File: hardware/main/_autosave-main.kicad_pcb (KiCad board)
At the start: 2 copper layers, 120 parts, among them J1 RJ45, J2 RJ45, J401 USART, J601 RJ45, J602 RJ45, K1 DIPxx-1Axx-13x, K2 SANYOU_SRD_Form_C, Q1 Q_NPN_BEC, Q2 BCV27, Q3 BCV27, U1 LM324, U2 LM324, U201 MCP2551-I/SN, U202 MCP2515-xSO, U401 ATMEGA328P-PU, U501 LM7805, Y201 16MHz, Y401 16MHz

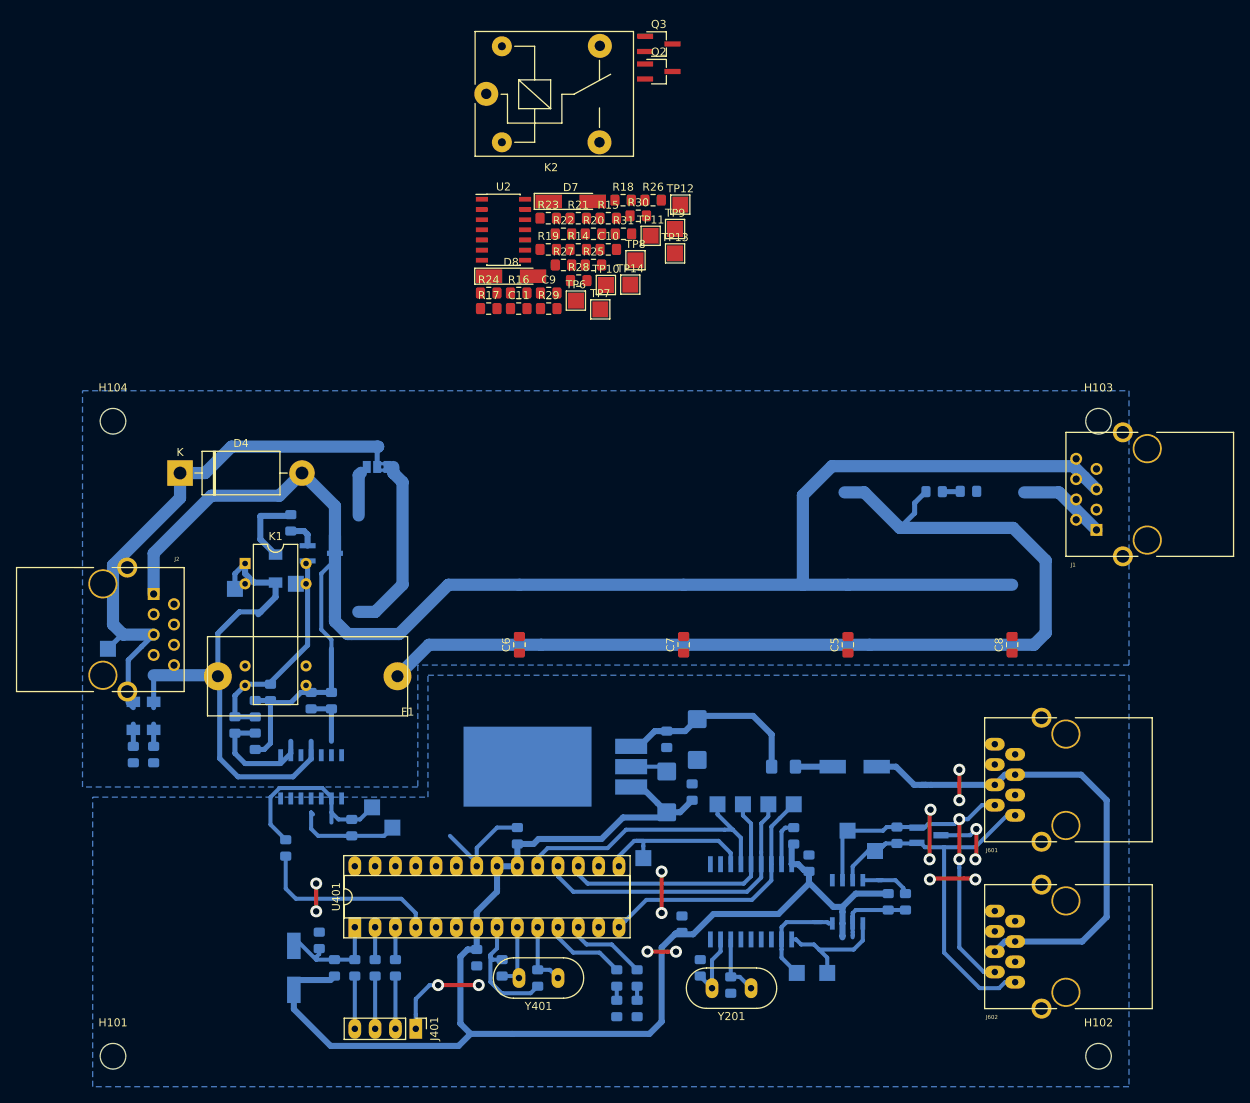
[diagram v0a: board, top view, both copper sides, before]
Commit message: Esquematico primeira versão Erro de referencia dos componentes na PCB com os do Esquematico solucionados
Pontos de teste adicionados
Alimentar o analog com +12V
Adicionar Snubber para os reles
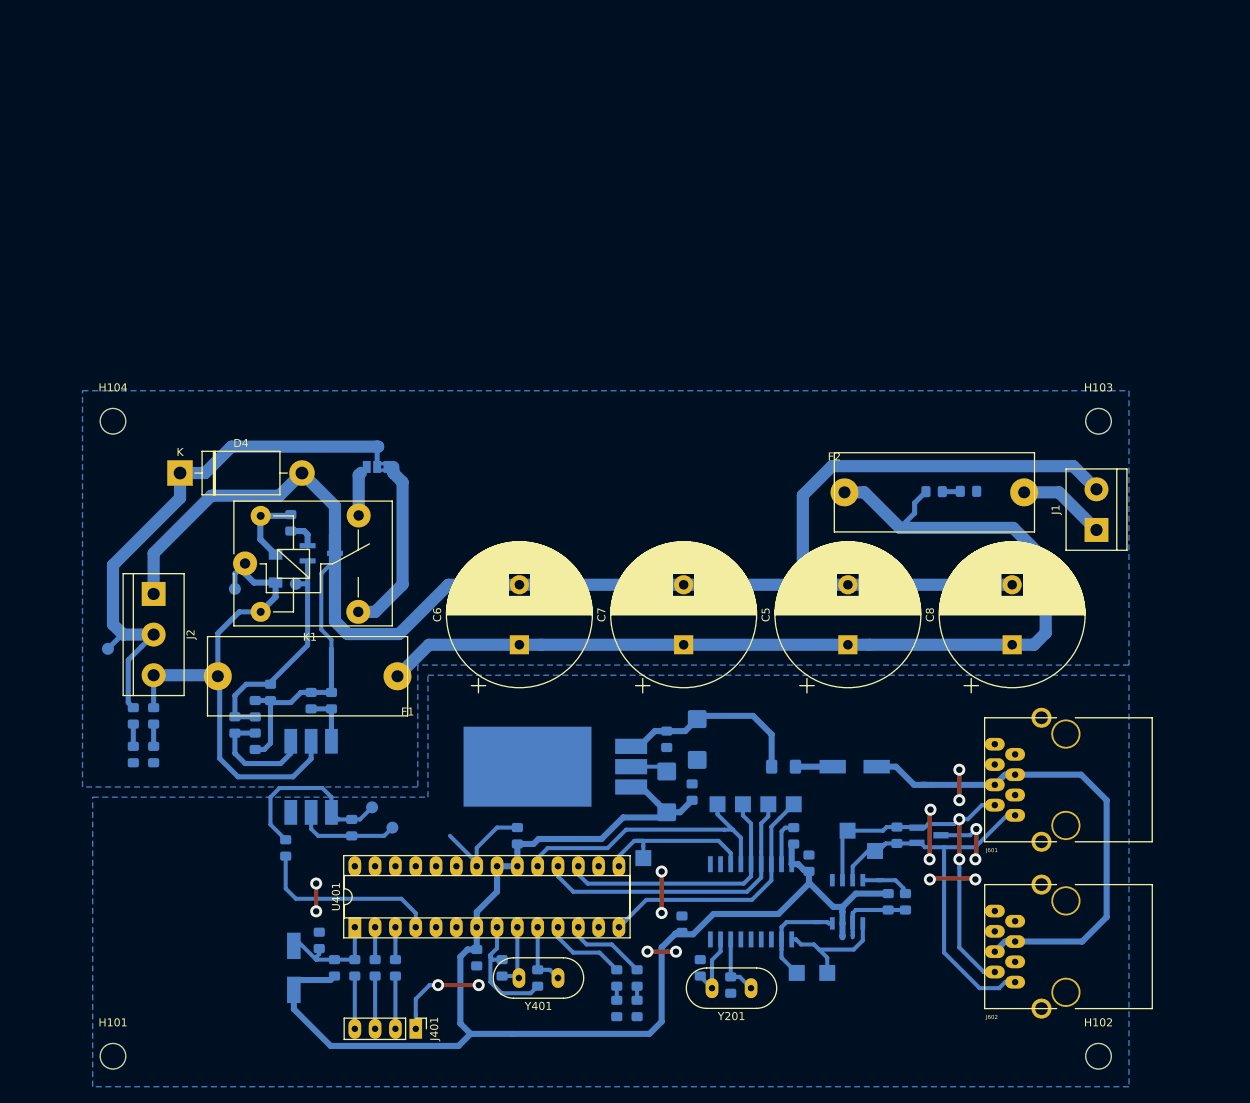
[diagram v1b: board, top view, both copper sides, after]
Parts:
- removed C10, C11, C9: 100n, Capacitor_SMD:C_0805_2012Metric_Pad1.15x1.40mm_HandSolder
- removed D7, D8: 4V7, Diode_SMD:D_MiniMELF_Handsoldering
- removed K2: SANYOU_SRD_Form_C, Relay_THT:Relay_SPDT_SANYOU_SRD_Series_Form_C
- removed Q2, Q3: BCV27, Package_TO_SOT_SMD:TSOT-23_HandSoldering
- removed R14, R15: 100k, Resistor_SMD:R_0805_2012Metric_Pad1.15x1.40mm_HandSolder
- removed R16, R17, R18, R19, R20, R21, R22, R23, R24, R25: 10k, Resistor_SMD:R_0805_2012Metric_Pad1.15x1.40mm_HandSolder
- removed R26, R27, R28, R29, R30, R31: 1k, Resistor_SMD:R_0805_2012Metric_Pad1.15x1.40mm_HandSolder
- removed TP10, TP9: op_a_out, TestPoint:TestPoint_Pad_2.0x2.0mm
- removed TP11, TP12: op_b_in+, TestPoint:TestPoint_Pad_2.0x2.0mm
- removed TP13, TP14: op_b_out, TestPoint:TestPoint_Pad_2.0x2.0mm
- removed TP6, TP8: op_a_in+, TestPoint:TestPoint_Pad_2.0x2.0mm
- removed TP7: op_a_in-, TestPoint:TestPoint_Pad_2.0x2.0mm
- removed U2: LM324, Package_SO:SOIC-14_3.9x8.7mm_P1.27mm
- added F2: 10A, KicadZeniteSolarLibrary18:Fuse_Holder_5x20, F.Cu at (170.2, 48.4)
- C1: value C_Small -> 100n
- C2: value 100n -> 1n
- C5, C6, C7, C8: value 100n -> 4700u 35V; footprint Capacitor_SMD:C_0805_2012Metric_Pad1.15x1.40mm_HandSolder -> Capacitor_THT:CP_Radial_D18.0mm_P7.50mm
- D1: value LL4148 -> G3mm; footprint Diode_SMD:D_MiniMELF -> LED_SMD:LED_0805_2012Metric_Pad1.15x1.40mm_HandSolder
- D3: value LL4148 -> R3mm; footprint Diode_SMD:D_MiniMELF -> LED_SMD:LED_0805_2012Metric_Pad1.15x1.40mm_HandSolder
- D4: value RED_LED -> MUR460
- D5: value GRN_LED -> G3mm
- F1: value Fuse Mega 200A -> 3A
- J1: value RJ45 -> Screw_Terminal_01x02; footprint KicadZeniteSolarLibrary18:RJ45_YH59_01 -> TerminalBlock:TerminalBlock_bornier-2_P5.08mm
- J2: value RJ45 -> Screw_Terminal_01x03; footprint KicadZeniteSolarLibrary18:RJ45_YH59_01 -> TerminalBlock:TerminalBlock_bornier-3_P5.08mm
- JP1: value Jp_TEST -> SolderJumper_3_Bridged12
- K1: value DIPxx-1Axx-13x -> coil: 12VDC, contact: 125V/10A; footprint Relay_THT:Relay_StandexMeder_DIP_LowProfile -> Relay_THT:Relay_SPDT_SANYOU_SRD_Series_Form_C
- Q1: value Q_NPN_BEC -> BCV27
- R1: value 1k2 -> 330R
- R2: value 1k2 -> NC
- R3: value 10k -> 1k2
- R4, R8: value 10k -> 1k
- R5: value 120 -> 10k
- R6: value 120 -> 120R
- R7: value 120 -> 1k
- TP1: value in- -> A1; footprint TestPoint:TestPoint_Pad_2.0x2.0mm -> TestPoint:TestPoint_Pad_D1.5mm
- TP2: value in+ -> K1; footprint TestPoint:TestPoint_Pad_2.0x2.0mm -> TestPoint:TestPoint_Pad_D1.5mm
- TP3: value in- -> 12V; footprint TestPoint:TestPoint_Pad_2.0x2.0mm -> TestPoint:TestPoint_Pad_D1.5mm
- TP4: value in+ -> B1; footprint TestPoint:TestPoint_Pad_2.0x2.0mm -> TestPoint:TestPoint_Pad_D1.5mm
- TP5: value op_a_in- -> OUT1; footprint TestPoint:TestPoint_Pad_2.0x2.0mm -> TestPoint:TestPoint_Pad_D1.5mm
- U1: value LM324 -> 4N25; footprint Package_SO:SOIC-14_3.9x8.7mm_P1.27mm -> Package_DIP:DIP-6_W8.89mm_SMDSocket_LongPads
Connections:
- net /MCU/CAN_CTRL renamed Net-(U401-Pad23)
- net /MCU/RL_OFF renamed Net-(U401-Pad24)
- C1 pad 2: GNDPWR -> GND
- C2 pad 1: Net-(C2-Pad1) -> GNDPWR
- C2 pad 2: GNDPWR -> Net-(C2-Pad2)
- C4 pad 2: GND -> GNDPWR
- C5 pad 1: Net-(C5-Pad1) -> +12V
- C5 pad 2: GND -> GNDPWR
- C6 pad 1: Net-(C6-Pad1) -> +12V
- C6 pad 2: /MCU/BAT_SIG -> GNDPWR
- C7 pad 1: Net-(C7-Pad1) -> +12V
- C7 pad 2: /MCU/CAP_SIG -> GNDPWR
- C8 pad 1: Net-(C8-Pad1) -> +12V
- C8 pad 2: GND -> GNDPWR
- D1 pad 1: +12V -> Net-(D1-Pad1)
- D1 pad 2: Net-(D1-Pad2) -> /pump_driver/Level_sensor
- D2 pad 1: +12V -> /pump_driver/Level_sensor
- D3 pad 1: +12V -> Net-(D3-Pad1)
- D3 pad 2: Net-(D3-Pad2) -> /pump_driver/+Pump
- D4 pad 1: GNDPWR -> /pump_driver/+Pump
- D4 pad 2: Net-(D4-Pad2) -> GNDPWR
- D5 pad 1: GNDPWR -> Net-(D5-Pad1)
- D5 pad 2: Net-(D5-Pad2) -> +12V
- F1 pad 1: /+BAT -> +12V
- F1 pad 2: /charger/Unfused_Bat+ -> /pump_driver/Level_sensor
- J1 pad 1: /CANBUS CONN/CAN_H -> /filter/Vin
- J1 pad 2: /CANBUS CONN/CAN_L -> GNDPWR
- J2 pad 1: /CANBUS CONN/CAN_H -> GNDPWR
- J2 pad 2: /CANBUS CONN/CAN_L -> /pump_driver/+Pump
- J2 pad 3: GND -> /pump_driver/Level_sensor
- JP1 pad 1: /+BAT -> Net-(JP1-Pad1)
- JP1 pad 2: /analog/in1+ -> /pump_driver/+Pump
- JP1 pad 3: (no net) -> Net-(JP1-Pad3)
- K1 pad 1: +12V -> /pump_driver/Level_sensor
- K1 pad 2: Net-(K1-Pad2) -> /pump_driver/Level_sensor
- Q1 pad 1: Net-(C1-Pad1) -> Net-(C4-Pad1)
- Q1 pad 2: GNDPWR -> Net-(Q1-Pad2)
- Q1 pad 3: /charger/S_RL_ON -> GNDPWR
- R1 pad 2: /MCU/Charge -> /MCU/ON_OFF_PUMP
- R2 pad 1: Net-(C2-Pad1) -> GNDPWR
- R2 pad 2: /MCU/RL_ON -> Net-(C2-Pad2)
- R3 pad 1: Net-(C1-Pad1) -> Net-(C4-Pad1)
- R3 pad 2: GNDPWR -> Net-(C3-Pad1)
- R4 pad 1: Net-(C2-Pad1) -> GNDPWR
- R4 pad 2: GNDPWR -> Net-(D1-Pad1)
- R5 pad 1: Net-(D2-Pad2) -> GNDPWR
- R5 pad 2: /charger/S_RL_ON -> Net-(C4-Pad1)
- R6 pad 1: Net-(K1-Pad3) -> Net-(Q1-Pad2)
- R6 pad 2: Net-(D1-Pad2) -> Net-(D2-Pad2)
- R7 pad 1: Net-(K1-Pad2) -> GNDPWR
- R7 pad 2: Net-(D3-Pad2) -> Net-(D3-Pad1)
- R8 pad 1: Net-(C3-Pad1) -> GNDPWR
- R8 pad 2: GNDPWR -> Net-(D5-Pad1)
- TP1 pad 1: Net-(R14-Pad1) -> Net-(C1-Pad1)
- TP2 pad 1: /analog/in1+ -> GND
- TP3 pad 1: Net-(R15-Pad1) -> /pump_driver/Level_sensor
- TP4 pad 1: /analog/in2+ -> Net-(C4-Pad1)
- TP5 pad 1: Net-(R18-Pad1) -> /pump_driver/+Pump
- U1 pad 1: (no net) -> Net-(C1-Pad1)
- U1 pad 2: (no net) -> GND
- U1 pad 3: (no net) -> Net-(U1-Pad3)
- U1 pad 4: +5V -> Net-(C3-Pad1)
- U1 pad 5: Net-(C8-Pad1) -> /pump_driver/Level_sensor
- U1 pad 6: /MCU/BAT_SIG -> Net-(C2-Pad2)
- U401 pad 25: /MCU/RL_ON -> Net-(U401-Pad25)
- U401 pad 26: /MCU/CAP_SIG -> Net-(U401-Pad26)
- U401 pad 27: /MCU/BAT_SIG -> Net-(U401-Pad27)
- U401 pad 28: /MCU/Charge -> Net-(U401-Pad28)
- U401 pad 4: Net-(U401-Pad4) -> /MCU/ON_OFF_PUMP
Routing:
- net Net-(JP1-Pad1): track 0.00 -> 22.1 mm
- net /+BAT: track 22.1 -> 0.00 mm
- net GND: track 108.8 -> 91.7 mm, vias 16 -> 10
- net /CANBUS CONN/CAN_H: track 61.6 -> 50.6 mm
- net /filter/Vin: track 0.00 -> 11.0 mm
- net (no net): track 6.18 -> 17.1 mm, vias 0 -> 6
- net Net-(JP1-Pad3): track 0.00 -> 6.18 mm
- net GNDPWR: track 234.0 -> 231.7 mm
- net Net-(D5-Pad1): track 0.00 -> 2.26 mm
